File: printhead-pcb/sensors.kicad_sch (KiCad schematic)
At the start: 25 parts, among them J1 T0, J2 T1, J3 T2, J4 T3, U1 PSSI2021SAY, U2 PSSI2021SAY, U4 PSSI2021SAY, U5 ADS1015IDGS, U9 PSSI2021SAY

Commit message: circuit finished?
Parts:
- removed JP1, JP2, JP3, JP5: trim_en_jumper, symbol Jumper:SolderJumper_3_Open
- removed R16, R17, R7, R9: 680, symbol Device:R
- removed R19, R20: 1k6, symbol Device:R
- removed R3, R4, R6, R8: 1k, symbol Device:R_Trim
- removed U1, U2, U4, U9: PSSI2021SAY, Package_TO_SOT_SMD:SOT-353_SC-70-5, symbol Reference_Current:PSSI2021SAY
- added C4, C5, C6, C8: 0.1µF, Capacitor_SMD:C_0402_1005Metric, symbol Device:C
- added C7: 0.1µFC, Capacitor_SMD:C_0402_1005Metric, symbol Device:C
- added D3: BLUE, LED_SMD:LED_0805_2012Metric, symbol Device:LED
- added L2, L3, L4, L5: L, Inductor_SMD:L_0402_1005Metric, symbol Device:L
- added R11: 330, Resistor_SMD:R_0402_1005Metric, symbol Device:R
- added R25, R26: 1k8, Resistor_SMD:R_0402_1005Metric, symbol Device:R
- J5: renamed from J1; footprint (none) -> Connector_JST:JST_GH_SM02B-GHS-TB_1x02-1MP_P1.25mm_Horizontal
- J6: renamed from J2; footprint (none) -> Connector_JST:JST_GH_SM02B-GHS-TB_1x02-1MP_P1.25mm_Horizontal
- J7: renamed from J3; footprint (none) -> Connector_JST:JST_GH_SM02B-GHS-TB_1x02-1MP_P1.25mm_Horizontal
- J8: renamed from J4; footprint (none) -> Connector_JST:JST_GH_SM02B-GHS-TB_1x02-1MP_P1.25mm_Horizontal
- R20: renamed from R18; value 1k6 -> 1k8; footprint (none) -> Resistor_SMD:R_0402_1005Metric
- R21: value 1k6 -> 1k8; footprint (none) -> Resistor_SMD:R_0402_1005Metric
- renumbered U5 to U3
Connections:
- net ADC0: now also R20.2, R21.2, C4.1, C6.1, C7.1, C8.1, L2.2, L3.2, L4.2, L5.2, R25.2, R26.2; no longer J5.2 (Pin_2)
- net ADC1: no longer J6.2 (Pin_2)
- net ADC2: no longer J7.2 (Pin_2)
- net ADC3: no longer J8.2 (Pin_2)
- net AREF: now also R25.1, R26.1
- net GND: now also U3.1 (ADDR), C4.2, C5.2, C6.2, C7.2, C8.2, R11.1
- net SCL: now reaches U3.10 (SCL)
- net at U3.2 (ALERT/RDY): now also D3.2 (A)
- net SDA: now reaches U3.9 (SDA)
- net +5V renamed +3.3V
- net +3.3V: now also C5.1
- new net: D3.1 (K), R11.2
- new net TC0: J5.2 (Pin_2), L2.1, L3.1, L4.1, L5.1
- new net TC1: J6.2 (Pin_2)
- new net TC2: J7.2 (Pin_2)
- new net TC3: J8.2 (Pin_2)
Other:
- moved on the sheet: J5, J6, J7, J8, R20, U3

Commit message: layout
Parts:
- removed L5: L, Inductor_SMD:L_0402_1005Metric, symbol Device:L
- added L1: L, Inductor_SMD:L_0603_1608Metric, symbol Device:L
- J6: renamed from J5; footprint Connector_JST:JST_GH_SM02B-GHS-TB_1x02-1MP_P1.25mm_Horizontal -> Connector_JST:JST_EH_S2B-EH_1x02_P2.50mm_Horizontal
- J7: renamed from J6; footprint Connector_JST:JST_GH_SM02B-GHS-TB_1x02-1MP_P1.25mm_Horizontal -> Connector_JST:JST_EH_S2B-EH_1x02_P2.50mm_Horizontal
- J8: renamed from J7; footprint Connector_JST:JST_GH_SM02B-GHS-TB_1x02-1MP_P1.25mm_Horizontal -> Connector_JST:JST_EH_B2B-EH-A_1x02_P2.50mm_Vertical
- J9: renamed from J8; footprint Connector_JST:JST_GH_SM02B-GHS-TB_1x02-1MP_P1.25mm_Horizontal -> Connector_JST:JST_EH_B2B-EH-A_1x02_P2.50mm_Vertical
- L2, L3, L4: footprint Inductor_SMD:L_0402_1005Metric -> Inductor_SMD:L_0603_1608Metric
- R12: renamed from R20; value 1k8 -> 4k7
- R13: renamed from R21; value 1k8 -> 4k7
- R15: renamed from R25; value 1k8 -> 4k7
- R16: renamed from R26; value 1k8 -> 4k7
- renumbered C7 to C10, C8 to C11, C4 to C7, C5 to C8, C6 to C9, D3 to D2, R11 to R14
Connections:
- net ADC0: now also L1.2; no longer C10.1, C11.1, C9.1, L2.2, L3.2, L4.2, R13.2, R15.2, R16.2
- net ADC1: now also C9.1, L2.2, R13.2
- net ADC2: now also C10.1, L3.2, R15.2
- net ADC3: now also C11.1, L4.2, R16.2
- net TC0: now also L1.1; no longer L2.1, L3.1, L4.1
- net TC1: now also L2.1
- net TC2: now also L3.1
- net TC3: now also L4.1
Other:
- moved on the sheet: C10, C11, C7, C9

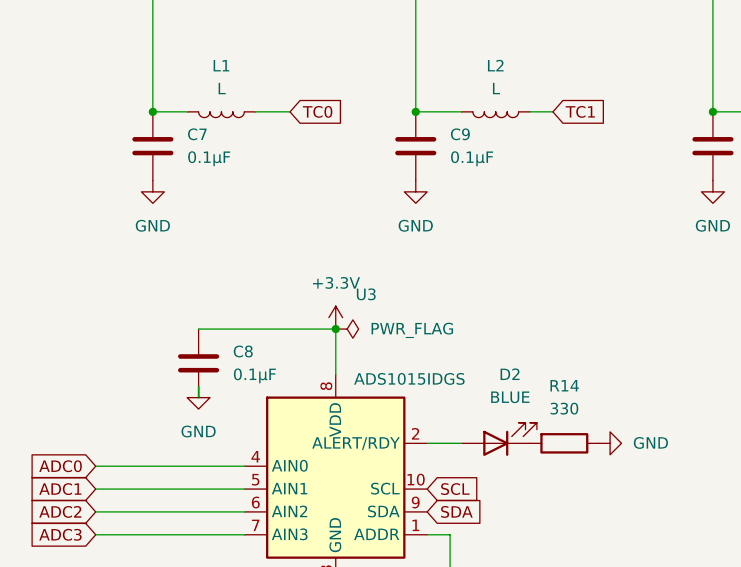
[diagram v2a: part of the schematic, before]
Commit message: rename datasheets
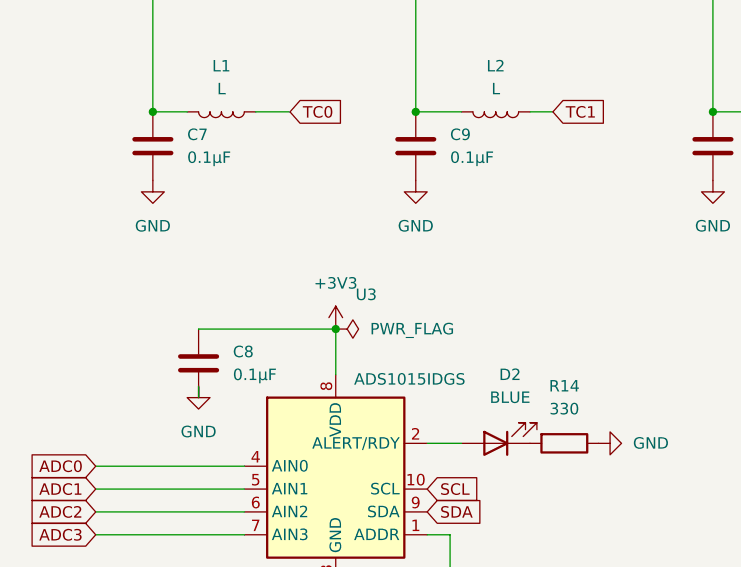
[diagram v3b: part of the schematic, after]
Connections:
- net +3.3V renamed +3V3
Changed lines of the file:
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@@
 			)
 		)
-		(property "Value" "+3.3V"
+		(property "Value" "+3V3"
 			(at 110.49 115.57 0)
 			(effects

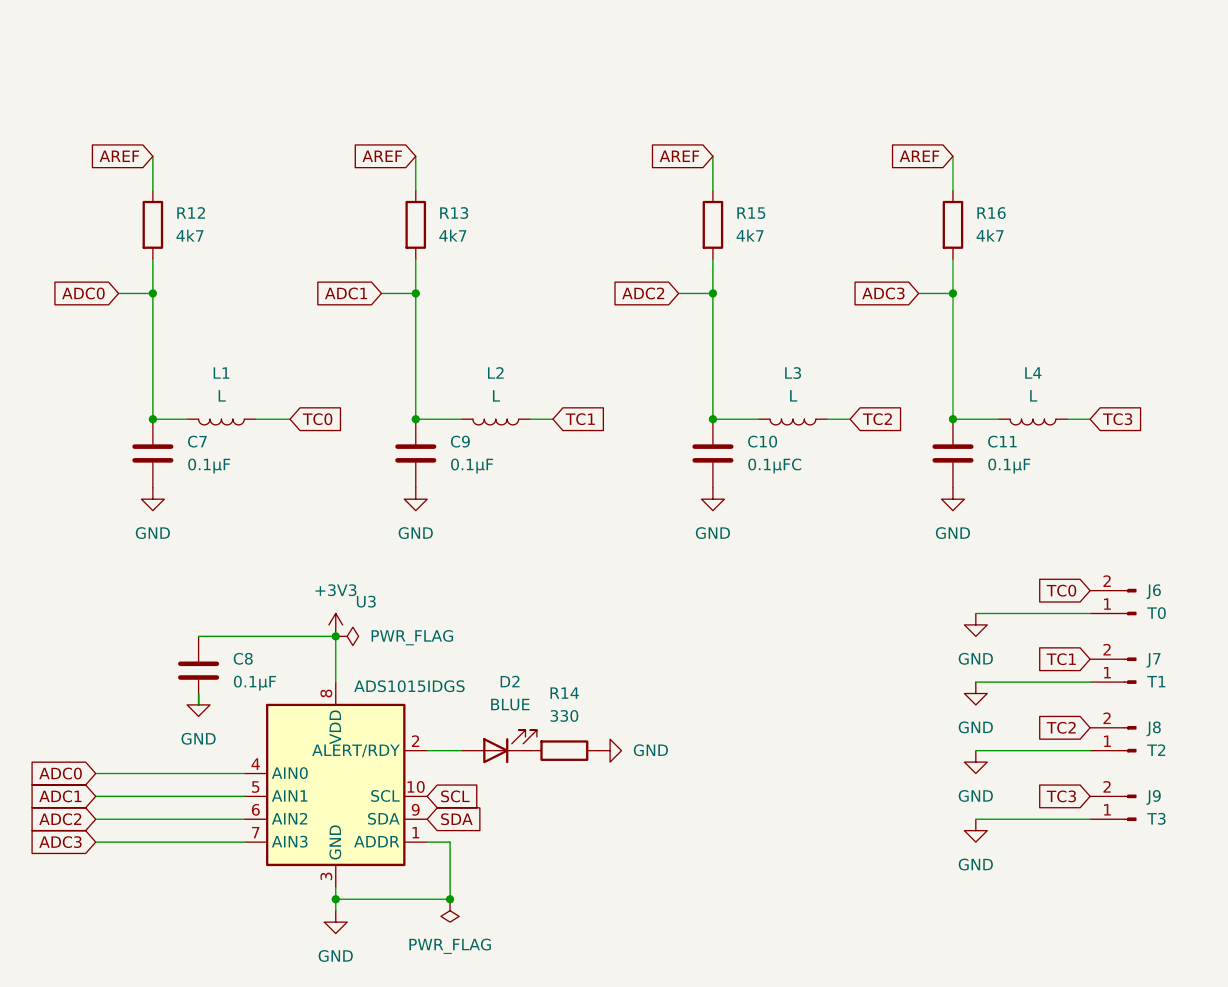
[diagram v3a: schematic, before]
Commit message: add pwr, gnd 5V for di2c chip
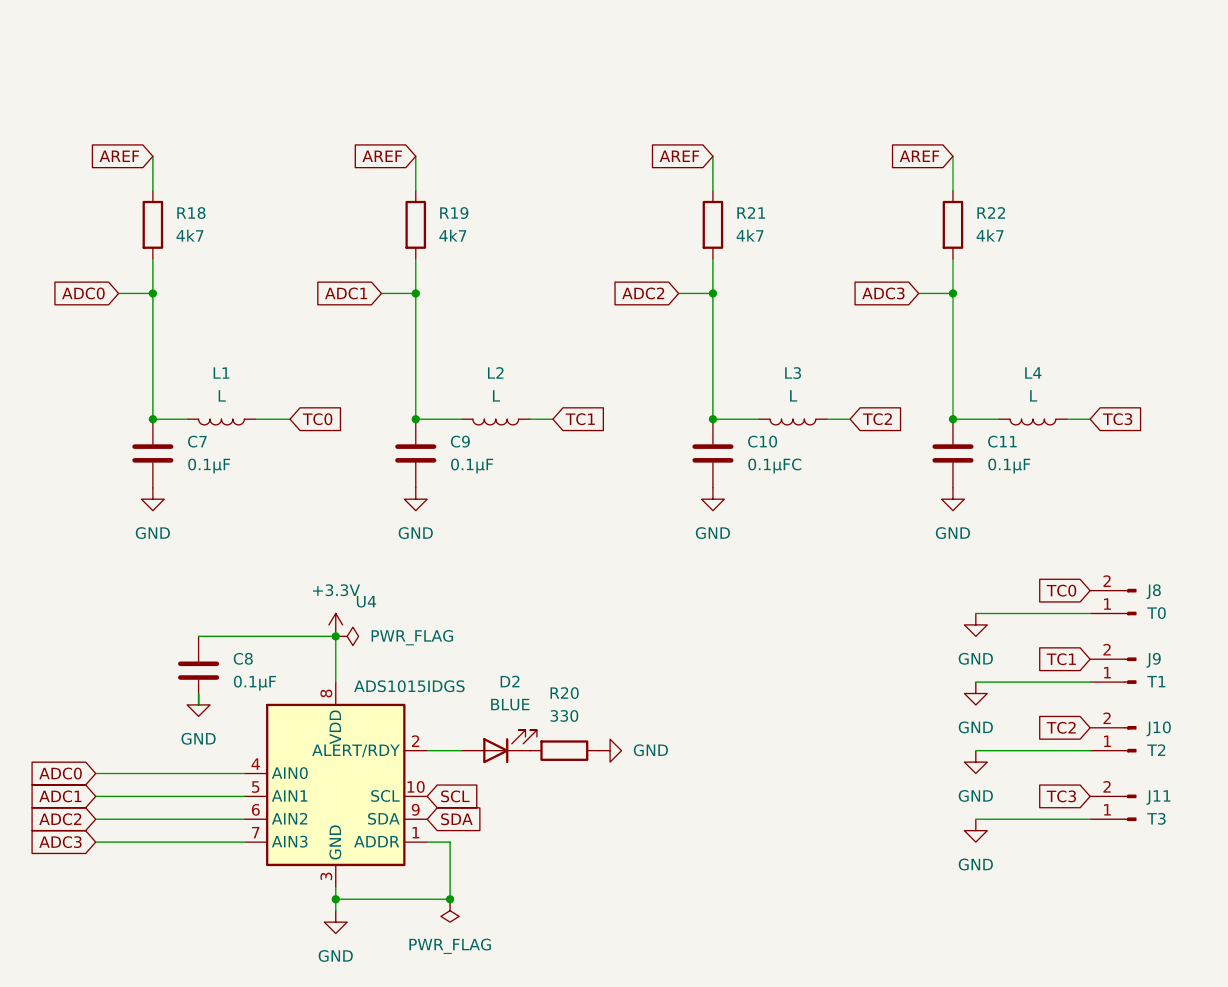
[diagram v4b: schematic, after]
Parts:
- renumbered J8 to J10, J9 to J11, J6 to J8, J7 to J9, R12 to R18, R13 to R19, R14 to R20, R15 to R21, R16 to R22, U3 to U4
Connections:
- net +3V3 renamed +3.3V
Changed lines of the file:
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@@
 		(dnp no)
 		(fields_autoplaced yes)
-		(property "Reference" "#PWR038"
+		(property "Reference" "#PWR042"
 			(at 110.49 157.48 0)
 			(effects
@@
 			(project "printhead-pcb"
 				(path "/813ad687-b864-44a5-b729-c4edf26b731d/d982b328-ddd9-44a5-ac14-a8d69a1e9eb0"
-					(reference "#PWR038")
+					(reference "#PWR042")
 					(unit 1)
 				)
@@
 		(dnp no)
 		(fields_autoplaced yes)
-		(property "Reference" "J8"
+		(property "Reference" "J10"
 			(at 200.66 130.8099 0)
 			(effects
@@
 			(project "printhead-pcb"
 				(path "/813ad687-b864-44a5-b729-c4edf26b731d/d982b328-ddd9-44a5-ac14-a8d69a1e9eb0"
-					(reference "J8")
+					(reference "J10")
 					(unit 1)
 				)
@@
 		(dnp no)
 		(fields_autoplaced yes)
-		(property "Reference" "#PWR040"
+		(property "Reference" "#PWR044"
 			(at 146.05 133.35 0)
 			(effects
@@
 			(project "printhead-pcb"
 				(path "/813ad687-b864-44a5-b729-c4edf26b731d/d982b328-ddd9-44a5-ac14-a8d69a1e9eb0"
-					(reference "#PWR040")
+					(reference "#PWR044")
 					(unit 1)
 				)
@@
 		(dnp no)
 		(fields_autoplaced yes)
-		(property "Reference" "J6"
+		(property "Reference" "J8"
 			(at 200.66 115.5699 0)
 			(effects
@@
 			(project "printhead-pcb"
 				(path "/813ad687-b864-44a5-b729-c4edf26b731d/d982b328-ddd9-44a5-ac14-a8d69a1e9eb0"
-					(reference "J6")
+					(reference "J8")
 					(unit 1)
 				)
@@
 		(dnp no)
 		(fields_autoplaced yes)
-		(property "Reference" "R16"
+		(property "Reference" "R22"
 			(at 181.61 73.6599 0)
 			(effects
@@
 			(project "printhead-pcb"
 				(path "/813ad687-b864-44a5-b729-c4edf26b731d/d982b328-ddd9-44a5-ac14-a8d69a1e9eb0"
-					(reference "R16")
+					(reference "R22")
 					(unit 1)
 				)
@@
 		(dnp no)
 		(fields_autoplaced yes)
-		(property "Reference" "J7"
+		(property "Reference" "J9"
 			(at 200.66 123.1899 0)
 			(effects
@@
 			(project "printhead-pcb"
 				(path "/813ad687-b864-44a5-b729-c4edf26b731d/d982b328-ddd9-44a5-ac14-a8d69a1e9eb0"
-					(reference "J7")
+					(reference "J9")
 					(unit 1)
 				)
@@
 		(dnp no)
 		(fields_autoplaced yes)
-		(property "Reference" "R15"
+		(property "Reference" "R21"
 			(at 154.94 73.6599 0)
 			(effects
@@
 			(project "printhead-pcb"
 				(path "/813ad687-b864-44a5-b729-c4edf26b731d/d982b328-ddd9-44a5-ac14-a8d69a1e9eb0"
-					(reference "R15")
+					(reference "R21")
 					(unit 1)
 				)
@@
 		(dnp no)
 		(fields_autoplaced yes)
-		(property "Reference" "#PWR045"
+		(property "Reference" "#PWR049"
 			(at 181.61 139.7 0)
 			(effects
@@
 			(project "printhead-pcb"
 				(path "/813ad687-b864-44a5-b729-c4edf26b731d/d982b328-ddd9-44a5-ac14-a8d69a1e9eb0"
-					(reference "#PWR045")
+					(reference "#PWR049")
 					(unit 1)
 				)
@@
 		(dnp no)
 		(fields_autoplaced yes)
-		(property "Reference" "R14"
+		(property "Reference" "R20"
 			(at 135.89 127 90)
 			(effects
@@
 			(project "printhead-pcb"
 				(path "/813ad687-b864-44a5-b729-c4edf26b731d/d982b328-ddd9-44a5-ac14-a8d69a1e9eb0"
-					(reference "R14")
+					(reference "R20")
 					(unit 1)
 				)
@@
 		(dnp no)
 		(fields_autoplaced yes)
-		(property "Reference" "#PWR046"
+		(property "Reference" "#PWR050"
 			(at 181.61 147.32 0)
 			(effects
@@
 			(project "printhead-pcb"
 				(path "/813ad687-b864-44a5-b729-c4edf26b731d/d982b328-ddd9-44a5-ac14-a8d69a1e9eb0"
-					(reference "#PWR046")
+					(reference "#PWR050")
 					(unit 1)
 				)
@@
 		(dnp no)
 		(fields_autoplaced yes)
-		(property "Reference" "#PWR036"
+		(property "Reference" "#PWR040"
 			(at 95.25 133.35 0)
 			(effects
@@
 			(project "printhead-pcb"
 				(path "/813ad687-b864-44a5-b729-c4edf26b731d/d982b328-ddd9-44a5-ac14-a8d69a1e9eb0"
-					(reference "#PWR036")
+					(reference "#PWR040")
 					(unit 1)
 				)
@@
 		(dnp no)
 		(fields_autoplaced yes)
-		(property "Reference" "R12"
+		(property "Reference" "R18"
 			(at 92.71 73.6599 0)
 			(effects
@@
 			(project "printhead-pcb"
 				(path "/813ad687-b864-44a5-b729-c4edf26b731d/d982b328-ddd9-44a5-ac14-a8d69a1e9eb0"
-					(reference "R12")
+					(reference "R18")
 					(unit 1)
 				)
@@
 		(dnp no)
 		(fields_autoplaced yes)
-		(property "Reference" "R13"
+		(property "Reference" "R19"
 			(at 121.92 73.6599 0)
 			(effects
@@
 			(project "printhead-pcb"
 				(path "/813ad687-b864-44a5-b729-c4edf26b731d/d982b328-ddd9-44a5-ac14-a8d69a1e9eb0"
-					(reference "R13")
+					(reference "R19")
 					(unit 1)
 				)
@@
 		(dnp no)
 		(fields_autoplaced yes)
-		(property "Reference" "J9"
+		(property "Reference" "J11"
 			(at 200.66 138.4299 0)
 			(effects
@@
 			(project "printhead-pcb"
 				(path "/813ad687-b864-44a5-b729-c4edf26b731d/d982b328-ddd9-44a5-ac14-a8d69a1e9eb0"
-					(reference "J9")
+					(reference "J11")
 					(unit 1)
 				)
@@
 		(dnp no)
 		(fields_autoplaced yes)
-		(property "Reference" "#PWR043"
+		(property "Reference" "#PWR047"
 			(at 181.61 124.46 0)
 			(effects
@@
 			(project "printhead-pcb"
 				(path "/813ad687-b864-44a5-b729-c4edf26b731d/d982b328-ddd9-44a5-ac14-a8d69a1e9eb0"
-					(reference "#PWR043")
+					(reference "#PWR047")
 					(unit 1)
 				)
@@
 		(dnp no)
 		(fields_autoplaced yes)
-		(property "Reference" "#PWR037"
+		(property "Reference" "#PWR041"
 			(at 110.49 124.46 0)
 			(effects
@@
 			)
 		)
-		(property "Value" "+3V3"
+		(property "Value" "+3.3V"
 			(at 110.49 115.57 0)
 			(effects
@@
 			(project "printhead-pcb"
 				(path "/813ad687-b864-44a5-b729-c4edf26b731d/d982b328-ddd9-44a5-ac14-a8d69a1e9eb0"
-					(reference "#PWR037")
+					(reference "#PWR041")
 					(unit 1)
 				)
@@
 		(on_board yes)
 		(dnp no)
-		(property "Reference" "U3"
+		(property "Reference" "U4"
 			(at 112.6841 116.84 0)
 			(effects
@@
 			(project "printhead-pcb"
 				(path "/813ad687-b864-44a5-b729-c4edf26b731d/d982b328-ddd9-44a5-ac14-a8d69a1e9eb0"
-					(reference "U3")
+					(reference "U4")
 					(unit 1)
 				)
@@
 		(dnp no)
 		(fields_autoplaced yes)
-		(property "Reference" "#PWR035"
+		(property "Reference" "#PWR039"
 			(at 90.17 110.49 0)
 			(effects
@@
 			(project "printhead-pcb"
 				(path "/813ad687-b864-44a5-b729-c4edf26b731d/d982b328-ddd9-44a5-ac14-a8d69a1e9eb0"
-					(reference "#PWR035")
+					(reference "#PWR039")
 					(unit 1)
 				)
@@
 		(dnp no)
 		(fields_autoplaced yes)
-		(property "Reference" "#PWR042"
+		(property "Reference" "#PWR046"
 			(at 179.07 110.49 0)
 			(effects
@@
 			(project "printhead-pcb"
 				(path "/813ad687-b864-44a5-b729-c4edf26b731d/d982b328-ddd9-44a5-ac14-a8d69a1e9eb0"
-					(reference "#PWR042")
+					(reference "#PWR046")
 					(unit 1)
 				)
@@
 		(dnp no)
 		(fields_autoplaced yes)
-		(property "Reference" "#PWR041"
+		(property "Reference" "#PWR045"
 			(at 152.4 110.49 0)
 			(effects
@@
 			(project "printhead-pcb"
 				(path "/813ad687-b864-44a5-b729-c4edf26b731d/d982b328-ddd9-44a5-ac14-a8d69a1e9eb0"
-					(reference "#PWR041")
+					(reference "#PWR045")
 					(unit 1)
 				)
@@
 		(dnp no)
 		(fields_autoplaced yes)
-		(property "Reference" "#PWR039"
+		(property "Reference" "#PWR043"
 			(at 119.38 110.49 0)
 			(effects
@@
 			(project "printhead-pcb"
 				(path "/813ad687-b864-44a5-b729-c4edf26b731d/d982b328-ddd9-44a5-ac14-a8d69a1e9eb0"
-					(reference "#PWR039")
+					(reference "#PWR043")
 					(unit 1)
 				)
@@
 		(dnp no)
 		(fields_autoplaced yes)
-		(property "Reference" "#PWR044"
+		(property "Reference" "#PWR048"
 			(at 181.61 132.08 0)
 			(effects
@@
 			(project "printhead-pcb"
 				(path "/813ad687-b864-44a5-b729-c4edf26b731d/d982b328-ddd9-44a5-ac14-a8d69a1e9eb0"
-					(reference "#PWR044")
-					(unit 1)
-				)
+					(reference "#PWR048")
+					(unit 1)
+				)

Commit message: worked through errors and added data sheets
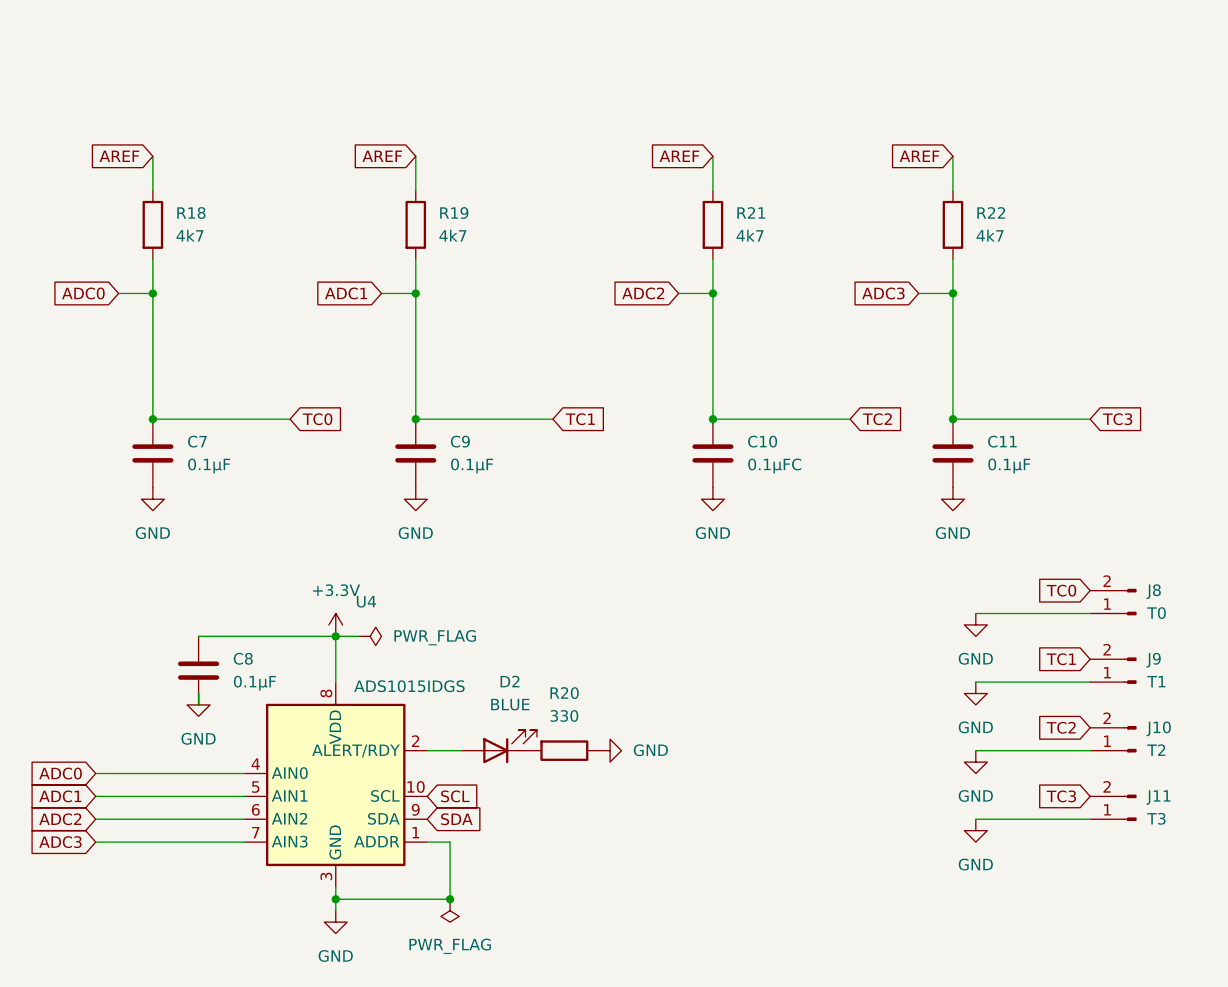
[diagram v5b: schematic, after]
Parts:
- removed L1, L2, L3, L4: L, Inductor_SMD:L_0603_1608Metric, symbol Device:L
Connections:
- net TC0 is gone; now on net ADC0: J8.2 (Pin_2)
- net TC1 is gone; now on net ADC1: J9.2 (Pin_2)
- net TC2 is gone; now on net ADC2: J10.2 (Pin_2)
- net TC3 is gone; now on net ADC3: J11.2 (Pin_2)
